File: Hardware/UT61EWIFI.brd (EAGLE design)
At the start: 94 x 27.9 mm, 18 parts, among them J1 ESPFLASH-2X3-1.27-SHROUDED, SW1 RESET

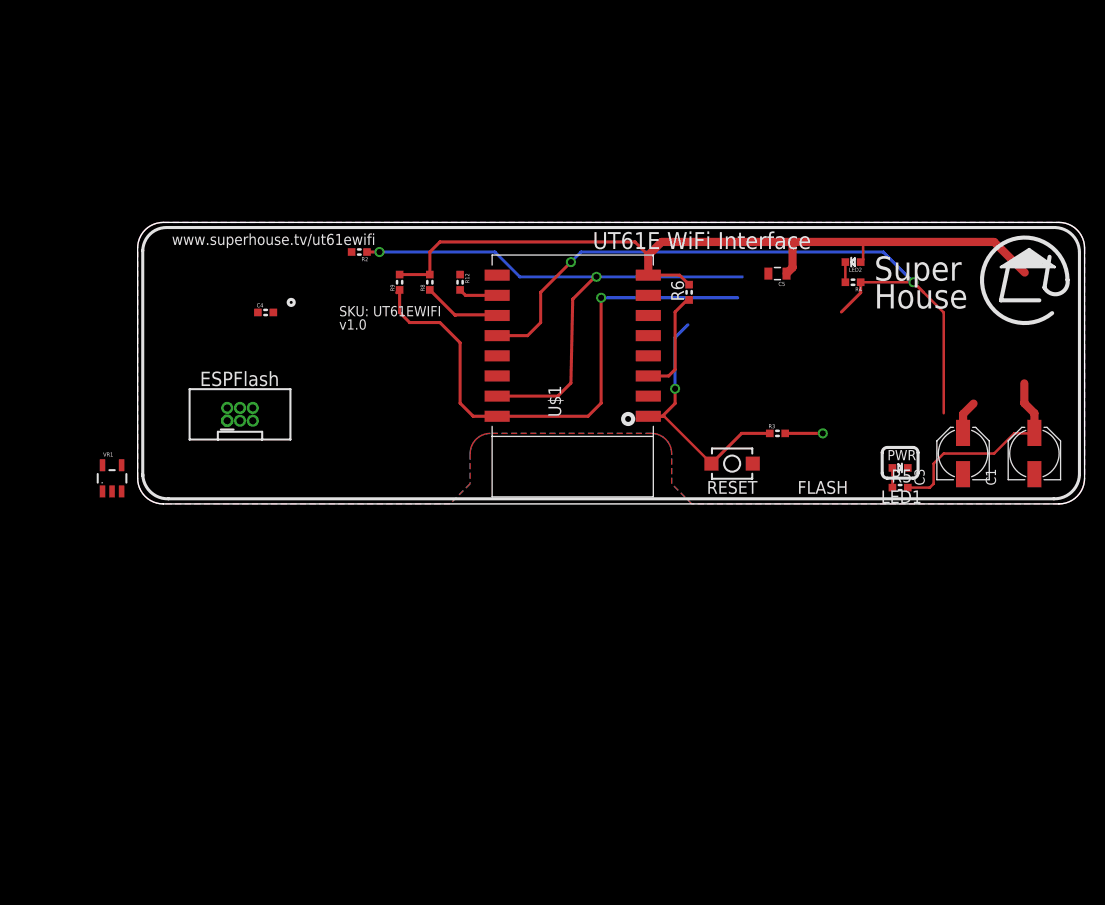
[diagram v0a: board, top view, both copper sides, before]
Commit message: Added voltage regulator. Added IR input.
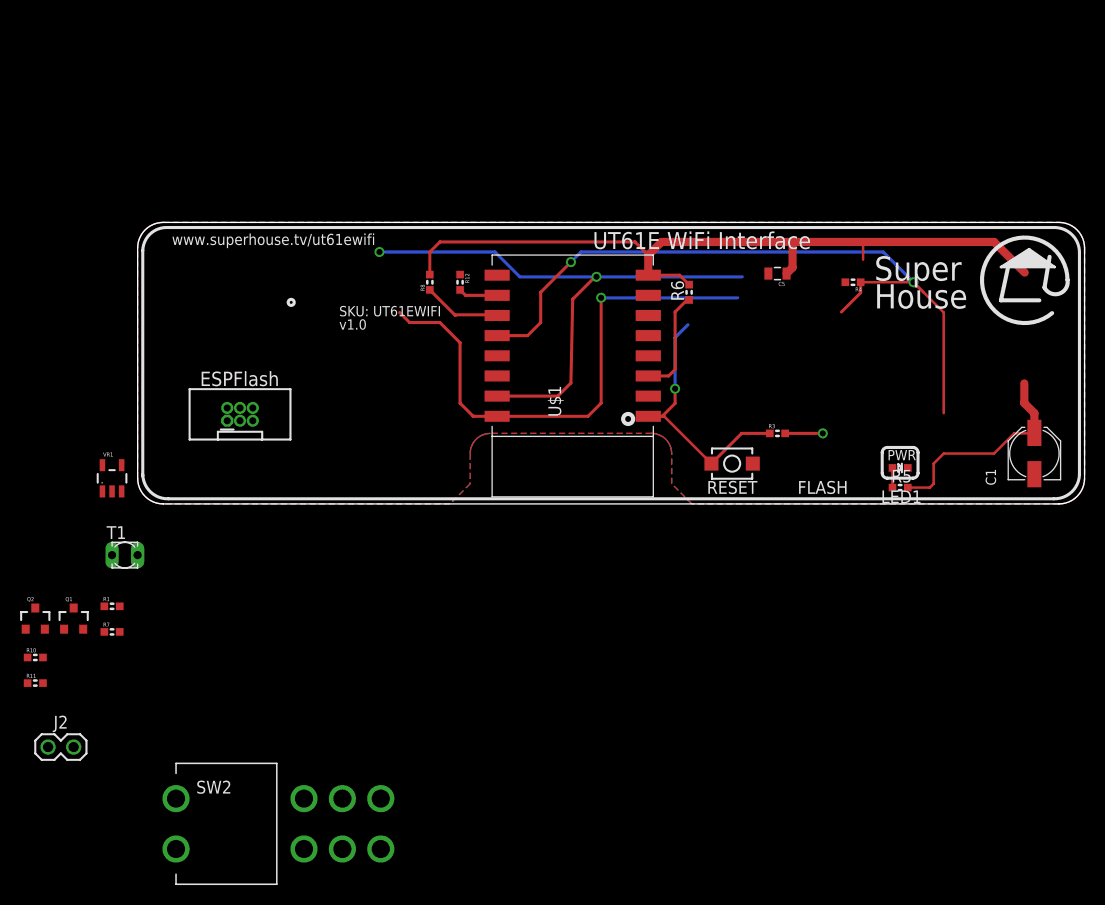
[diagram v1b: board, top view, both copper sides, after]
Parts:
- removed C3: 22uF 40V, SuperHouse-DiscreteSemi:PANASONIC_C
- removed C4: 100nF 50V, SuperHouse-DiscreteSemi:C0603
- removed LED2: RED, SuperHouse-LEDs:LED-0603
- removed R2: 1K, SuperHouse-DiscreteSemi:R0603
- removed R9: 4K7, SuperHouse-DiscreteSemi:R0603
- added J2: (no value), SuperHouse-Connectors:1X02
- added Q1, Q2: 2N7002, SuperHouse-DiscreteSemi:SOT23-3
- added R1, R11: 1K, SuperHouse-DiscreteSemi:R0603
- added R10, R7: 4K7, SuperHouse-DiscreteSemi:R0603
- added SW2: SWITCH-DPDT3, SuperHouse-Switches:7201SD9AV2BE
- added T1: BPX81, SuperHouse-Sensors:BPX81
- R4: value 1K -> 10K
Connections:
- removed net 12V: C3.+, C4.1
- removed net LINTX: R2.2
- removed net N$20: LED2.C, R4.2
- removed net RX: R2.1, U$1.15
- removed net TX: R9.1, U$1.16
- new net ESP_RX: J1.5, R11.2, U$1.15
- new net ESP_TX: J1.3, U$1.16
- new net N$1: Q2.3, R10.1, R11.1
- new net N$3: Q1.3, Q2.1, R7.1
- new net N$4: J2.2, SW2.2
- new net N$5: Q1.1, R1.1, T1.C
- new net N$6: SW2.3, VR1.1, VR1.3
- new net N$7: J2.1, SW2.5
- net !RST: now also J1.1
- net 3.3V: now also J1.2, R1.2, R10.2, R4.2, R7.2, VR1.5; no longer LED2.A, R9.2
- net GND: now also Q1.2, Q2.2, SW2.4, T1.E, VR1.2; no longer C3.-, C4.2
- net GPIO0: now also J1.6
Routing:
- net RX: track 57.7 -> 0.00 mm, vias 2 -> 0
- net ESP_RX: track 0.00 -> 56.5 mm, vias 0 -> 2
- net TX: track 55.2 -> 0.00 mm, vias 1 -> 0
- net ESP_TX: track 0.00 -> 52.3 mm, vias 0 -> 1
- net 12V: track 3.34 -> 0.00 mm
- net 3.3V: track 104.0 -> 100.7 mm
- net N$20: track 2.00 -> 0.00 mm

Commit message: Changed multimeter data pin from D0 to D5 for v1.1 release.
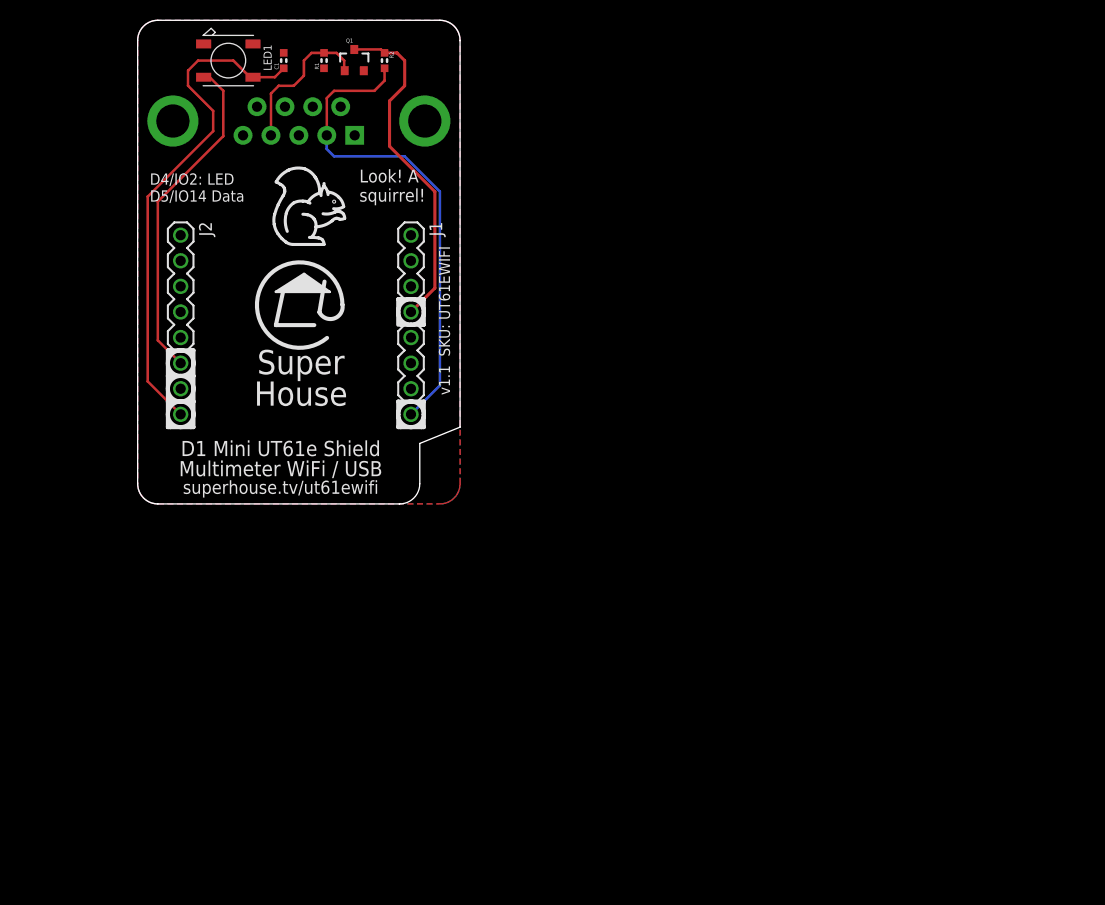
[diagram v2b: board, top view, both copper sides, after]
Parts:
- removed C5: 10uF, SuperHouse-DiscreteSemi:C0805
- removed Q2: 2N7002, SuperHouse-DiscreteSemi:SOT23-3
- removed R10, R7: 4K7, SuperHouse-DiscreteSemi:R0603
- removed R11: 1K, SuperHouse-DiscreteSemi:R0603
- removed R12, R3, R4, R6, R8: 10K, SuperHouse-DiscreteSemi:R0603
- removed R5: 2K2, SuperHouse-DiscreteSemi:R0603
- removed SW1: RESET, SuperHouse-Switches:TACTILE_SMT_3X4X2
- removed SW2: SWITCH-DPDT3, SuperHouse-Switches:7201SD9AV2BE
- removed T1: BPX81, SuperHouse-Sensors:BPX81
- removed U$1: ESP12-SMT, SuperHouse-MCUs:ESP12
- removed VR1: AP2112KSOT25, SuperHouse-Regulators:SOT23-5
- added J3: DB9-M, SuperHouse-Connectors:DB9-PCB-PLUG
- added R2: 10K, SuperHouse-Resistors:R0603
- C1: value 22uF 40V -> 1uF; device SuperHouse-DiscreteSemi:PANASONIC_C -> SuperHouse-Capacitors:C0603
- J1: value ESPFLASH-2X3-1.27-SHROUDED -> M08-PIN-BELOW; device SuperHouse-ESPFlash:2X3-1.27-SHROUDED -> SuperHouse-Connectors:1X08-P-BELOW
- J2: value (none) -> M08-PIN-BELOW; device SuperHouse-Connectors:1X02 -> SuperHouse-Connectors:1X08-P-BELOW
- LED1: value BLUE -> WS2812B; device SuperHouse-LEDs:LED-0603 -> SuperHouse-LEDs:WS2812B
- Q1: device SuperHouse-DiscreteSemi:SOT23-3 -> SuperHouse-Transistors:SOT23-3
- R1: value 1K -> 10K; device SuperHouse-DiscreteSemi:R0603 -> SuperHouse-Resistors:R0603
- moved C1 84.1 mm to (14.5, 44.0)
- moved LED1 78.0 mm to (9.00, 44.0)
- moved Q1 62.0 mm to (21.5, 44.0)
- moved R1 58.1 mm to (18.5, 44.0), turned to 90 degrees
- moved J2 43.6 mm to (4.27, 17.8), turned to 270 degrees
- moved J1 19.2 mm to (27.1, 17.8), turned to 270 degrees
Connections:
- removed net !RST: J1.1, R3.1, SW1.1, U$1.1
- removed net ADC: U$1.2
- removed net CH_PD: R6.1, U$1.3
- removed net ESP_RX: J1.5, R11.2, U$1.15
- removed net ESP_TX: J1.3, U$1.16
- removed net GPIO0: J1.6, R4.1, U$1.12
- removed net GPIO12: U$1.6
- removed net GPIO13: U$1.7
- removed net GPIO14: U$1.5
- removed net GPIO15: R12.2, U$1.10
- removed net GPIO16: U$1.4
- removed net GPIO2: R8.1, U$1.11
- removed net GPIO4: U$1.14
- removed net GPIO5: U$1.13
- removed net N$14: LED1.A, R5.1
- removed net N$3: Q1.3, Q2.1, R7.1
- removed net N$4: J2.2, SW2.2
- removed net N$5: Q1.1, R1.1, T1.C
- removed net N$6: SW2.3, VR1.1, VR1.3
- removed net N$7: J2.1, SW2.5
- new net 5V: C1.1, J2.8, LED1.1-VDD
- new net A0: J1.2
- new net D0_IO16: J1.3
- new net D1: J2.3
- new net D2: J2.4
- new net D3: J2.5
- new net D4_IO2_LED: J2.6, LED1.4-DIN
- new net D5_IO14_RXDATA: J1.4, Q1.3, R2.1
- new net D6: J1.5
- new net D7: J1.6
- new net D8: J1.7
- new net RST: J1.1
- new net RX: J2.2
- new net TX: J2.1
- net 3.3V: now also J1.8, J3.4, R2.2; no longer C1.+, C5.1, J1.2, R1.2, R10.2, R3.2, R4.2, R5.2, R6.2, R7.2, R8.2, U$1.8, VR1.5
- net GND: now also C1.2, J2.7, J3.5, J3.7, LED1.3-GND, R1.1; no longer C1.-, C5.2, J1.4, LED1.C, Q2.2, R12.1, SW1.2, SW2.4, T1.E, U$1.9, VR1.2
- net N$1: now also J3.2, Q1.1, R1.2; no longer Q2.3, R10.1, R11.1
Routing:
- net GPIO0: track 71.0 -> 0.00 mm, vias 2 -> 0
- net ESP_RX: track 56.5 -> 0.00 mm, vias 2 -> 0
- net ESP_TX: track 52.3 -> 0.00 mm, vias 1 -> 0
- net 3.3V: track 100.7 -> 49.0 mm, vias 1 -> 0
- net 5V: track 0.00 -> 50.2 mm
- net D5_IO14_RXDATA: track 0.00 -> 33.9 mm
- net D4_IO2_LED: track 0.00 -> 33.2 mm
- net !RST: track 25.4 -> 0.00 mm, vias 1 -> 0
- net N$1: track 0.00 -> 15.3 mm
- net CH_PD: track 10.5 -> 0.00 mm
- net GPIO2: track 7.83 -> 0.00 mm
- net GPIO15: track 3.90 -> 0.00 mm
- net N$14: track 1.95 -> 0.00 mm
- added copper zone on layer 16, net GND
- removed copper zone on layer 16, net 3.3V
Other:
- board size 94 x 27.9 mm -> 32 x 48 mm
- board text added: "(C)2021 SuperHouse Automation Pty Ltd Released under the TAPR Open Hardware License"
- board text added: "3.3V"
- board text added: "5V"
- board text added: "A0"
- board text added: "D0"
- board text added: "D1"
- board text added: "D1 Mini UT61e Shield"
- board text added: "D2"
- board text added: "D3"
- board text added: "D4"
- board text added: "D4/IO2: LED D5/IO14 Data"
- board text added: "D5"
- board text added: "D6"
- board text added: "D7"
- board text added: "D8"
- board text added: "GND"
- board text added: "Look! A squirrel!"
- board text added: "Multimeter WiFi / USB"
- board text added: "RST"
- board text added: "RX"
- board text added: "TX"
- board text added: "superhouse.tv/ut61ewifi"
- board text added: "v1.1 SKU: UT61EWIFI"
- board text removed: "(c) 2018 SuperHouse Automation Pty Ltd Released under the TAPR Open Hardware License www.tapr.org/OHL"
- board text removed: "A"
- board text removed: "CH_PD biased HIGH by default GPIO0 pulled LOW by FLASH"
- board text removed: "ESPFlash"
- board text removed: "FLASH"
- board text removed: "K"
- board text removed: "PWR"
- board text removed: "RESET"
- board text removed: "SKU: UT61EWIFI v1.0"
- board text removed: "UT61E WiFi Interface"
- board text removed: "www.superhouse.tv/ut61ewifi"
